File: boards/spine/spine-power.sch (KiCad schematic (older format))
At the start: 38 parts, among them Q3 IRFML8244, Q4 IRFML8244, U10 RT8299A, U11 TCR2EF12, U12 TCR2EF25, U8 NC7WZ14, U9 NC7WZ14

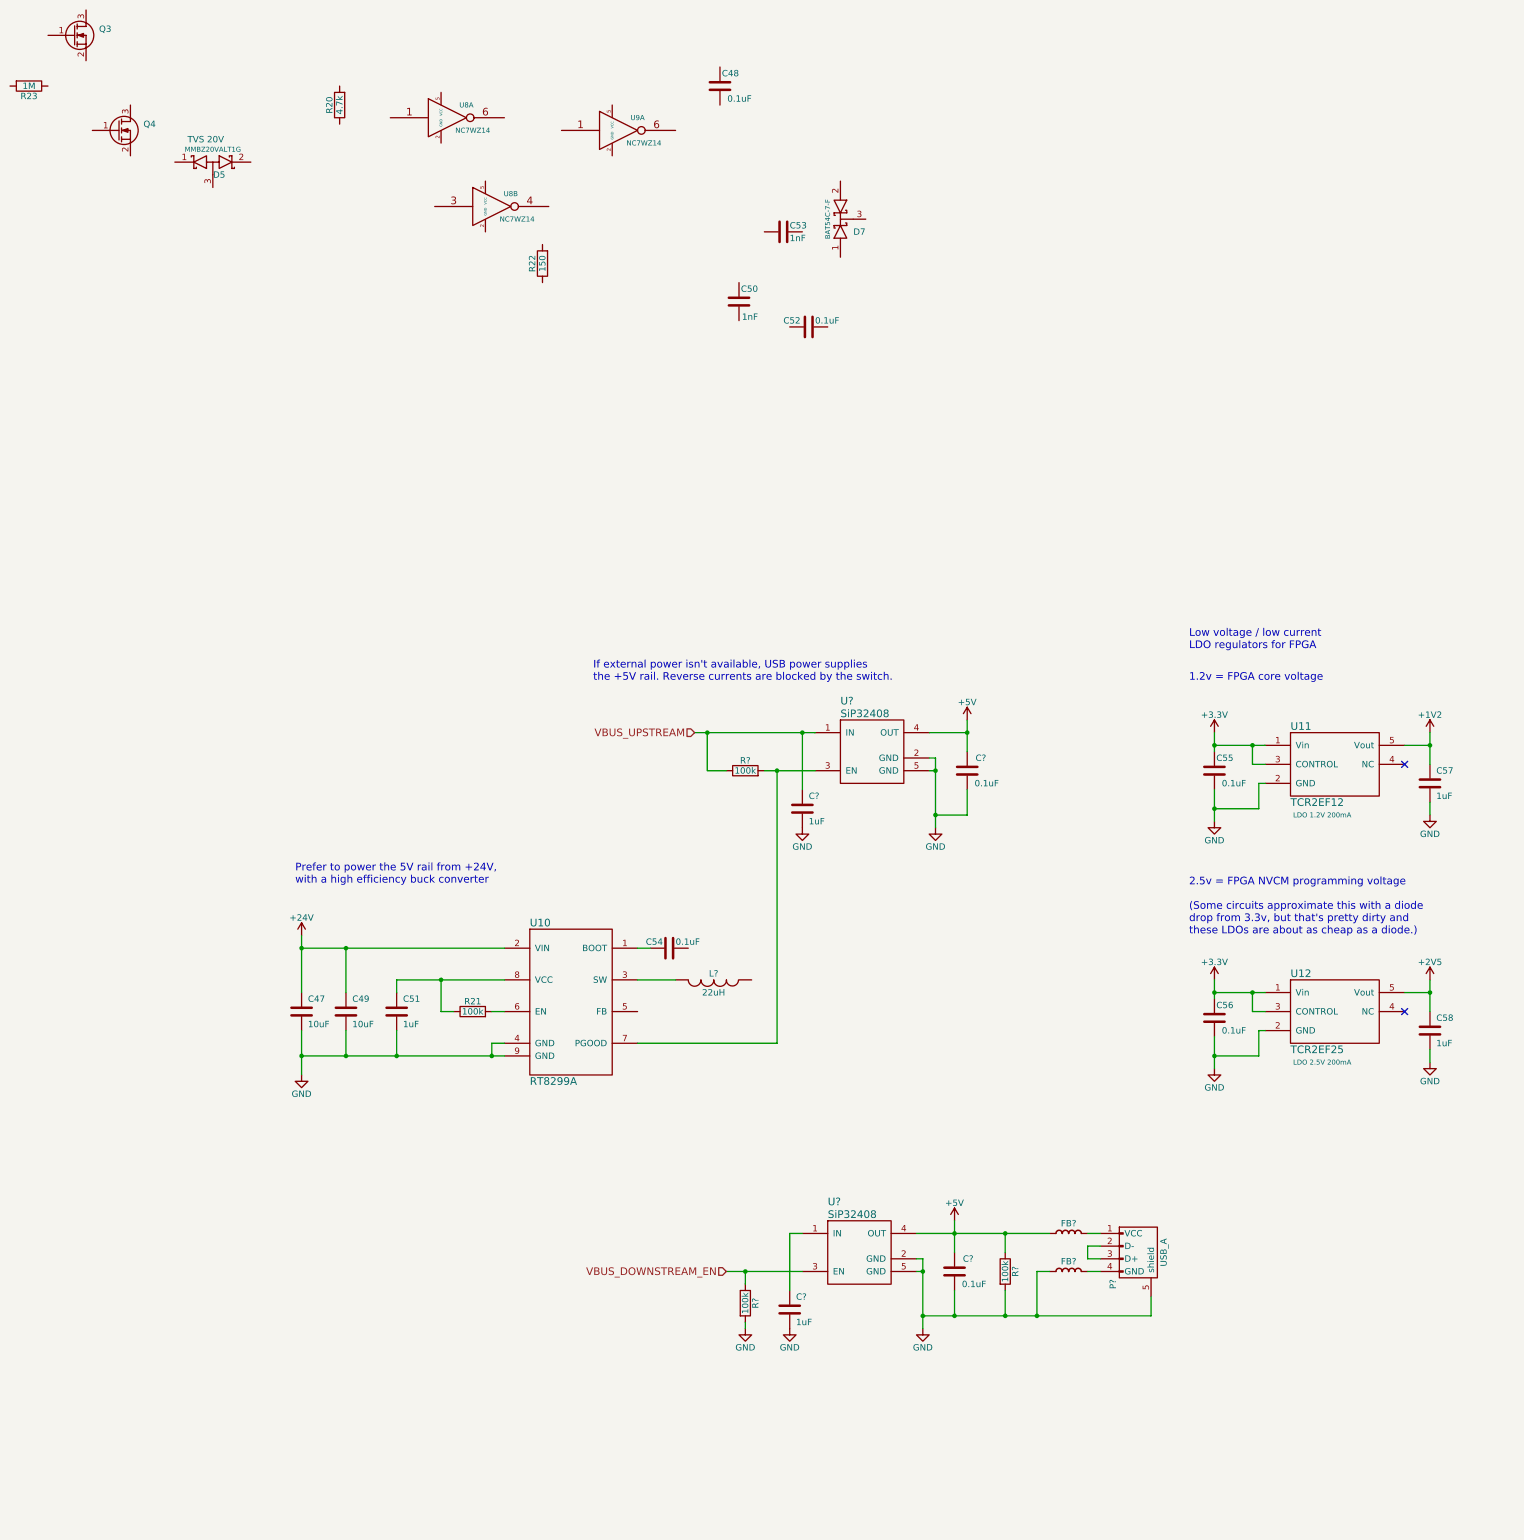
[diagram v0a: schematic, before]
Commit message: Split up the power schematic
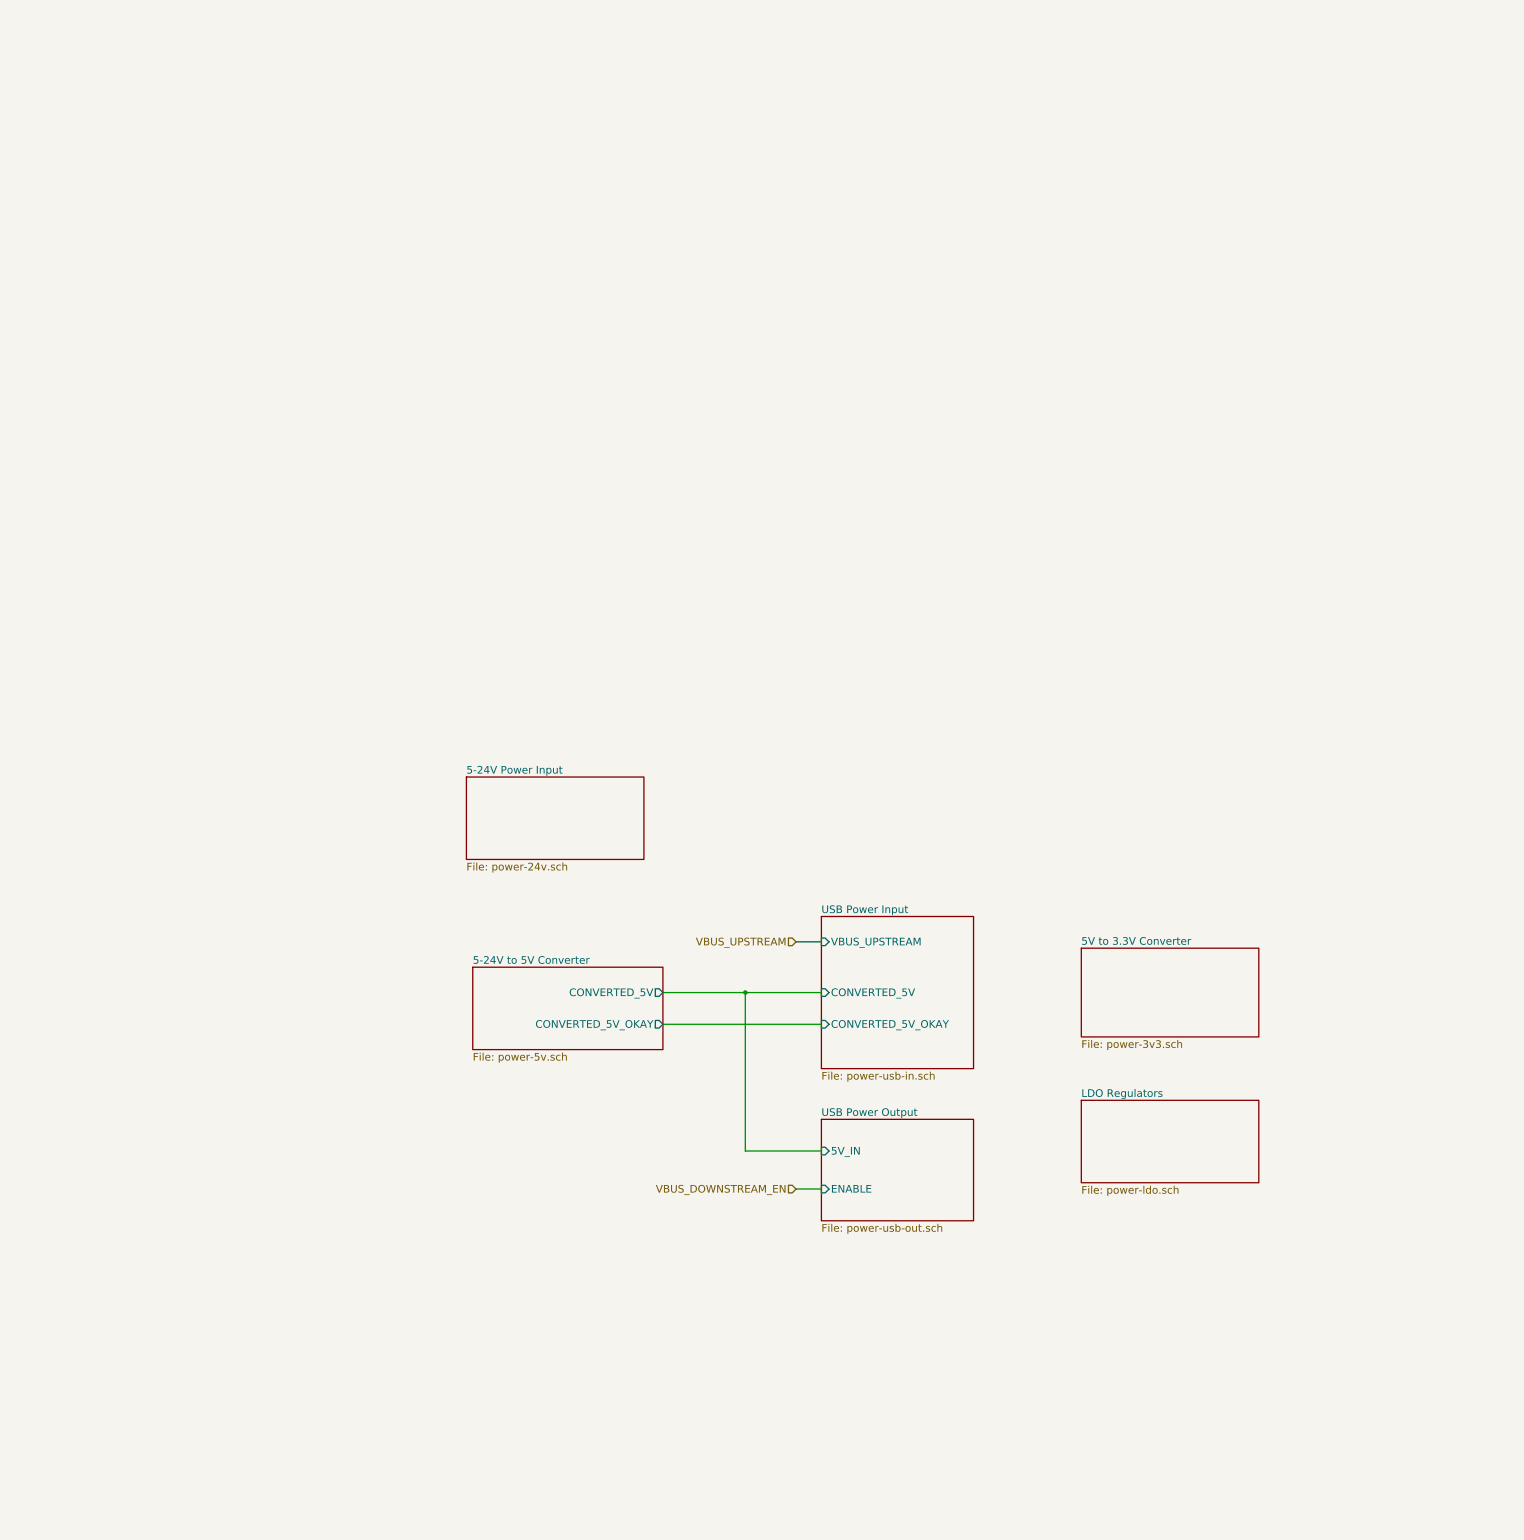
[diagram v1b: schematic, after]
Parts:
- removed C47, C49: 10uF, 1206, symbol C
- removed C48, C52, C54, C55, C56, C? (x2): 0.1uF, 0805, symbol C
- removed C50, C53: 1nF, 0805, symbol C
- removed C51, C57, C58, C? (x2): 1uF, 0805, symbol C
- removed D5: TVS 20V, symbol D_Schottky_x2_ACom_KKA
- removed D7: BAT54 2x common cathode, symbol D_Schottky_x2_KCom_AAK
- removed FB? (x2): Ferrite bead, symbol FERRITE_BEAD
- removed L?: 22uH, symbol INDUCTOR
- removed P?: USB_A, symbol USB_A
- removed Q3, Q4: IRFML8244, symbol Q_NMOS_GSD
- removed R20: 4.7k, symbol R
- removed R21, R? (x3): 100k, symbol R
- removed R22: 150, symbol R
- removed R23: 1M, symbol R
- removed U10: RT8299A, 8-SOP-EP, symbol RT8299A
- removed U11: TCR2EF12, SOT-753, symbol TCR2EF
- removed U12: TCR2EF25, SOT-753, symbol TCR2EF
- removed U8, U9: NC7WZ14, symbol NC7WZ14
- removed U? (x2): SiP32408, symbol SiP32408
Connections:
- no-connect marks 2 -> 0
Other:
- note removed: "1.2v = FPGA core voltage"
- note removed: "2.5v = FPGA NVCM programming voltage\n\n(Some circuits approximate this with a diode\ndrop from 3.3v, but that's pretty dirty and\nthese LDOs are about as cheap as a diode.)"
- note removed: "If external power isn't available, USB power supplies\nthe +5V rail. Reverse currents are blocked by the switch."
- note removed: "Low voltage / low current\nLDO regulators for FPGA"
- note removed: "Prefer to power the 5V rail from +24V,\nwith a high efficiency buck converter"

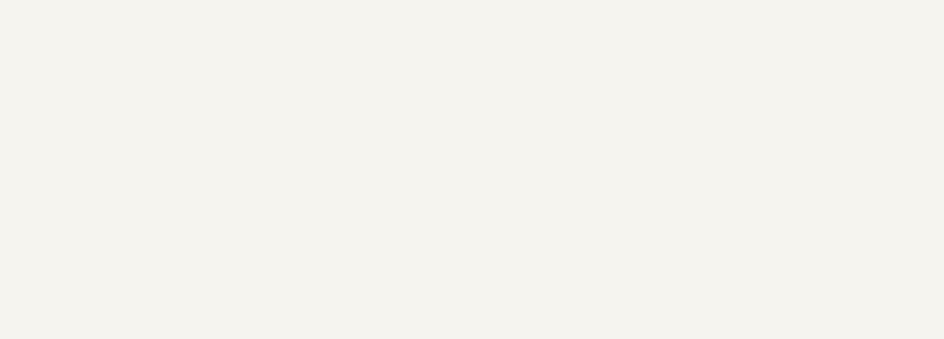
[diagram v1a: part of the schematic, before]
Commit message: Clock generator, sync connectors, title blocks
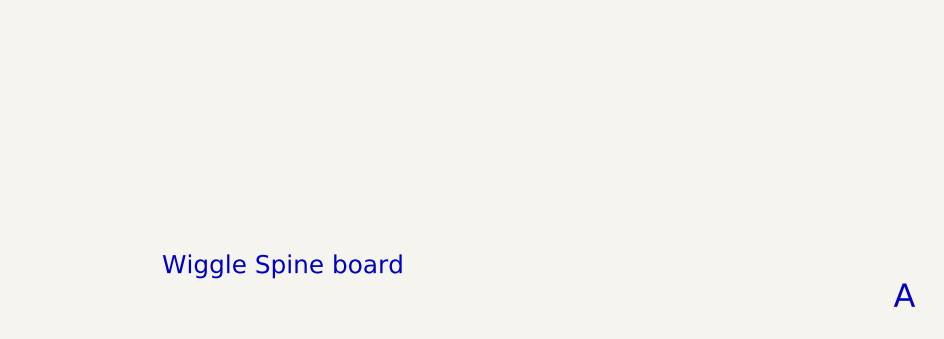
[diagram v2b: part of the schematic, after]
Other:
- note added: "A"
- note added: "Wiggle Spine board"
